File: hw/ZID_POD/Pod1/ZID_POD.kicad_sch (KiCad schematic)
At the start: 2 parts, among them J1 Z80-POD

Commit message: POD PCB 4 layouts
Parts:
- Z80-SKT1: renamed from SKT1; footprint Package_DIP:DIP-40_W15.24mm -> Package_DIP:DIP-40_W15.24mm_Socket; PIN_NOTE BIDIRECTIONAL pins are OUT on Z80, IN on DEBUGGER -> BIDIRECTIONAL pins are OUT on Z80, IN on TARGET
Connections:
- net GND: now also J1.30 (GND/NC)
- net PWR: no longer names the net of Z80-SKT1.11 (GND/NC)
- net PWR: no longer J1.30 (5V)
- no-connect marks 0 -> 1
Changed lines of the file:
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@@
 	(title_block
 		(title "ZID POD (1)")
-		(date "2026-04-10")
+		(date "2026-04-13")
 		(rev "PR1.0")
 		(company "SilkyDESIGN")
 		(comment 1 "Copyright 2026 AESilky")
+		(comment 3 "Z80 positions/orientations.")
+		(comment 4 "Layout 1 of 4 to accommodate different")
 	)
 	(text_box "NOTE: The ZID uses a FFC/FPC cable to connect to the POD. The Z80 signals are 1:1 on the ZID. Since the FFC cable is single side, it means the signal to pin on the POD connector are 1:40/40:1.\nThe Z80 Socket/Pins are 1:1. So, Pin-1 on the POD connector goes to Pin-40 on the Z80 Socket."
@@
 		)
 	)
+	(no_connect
+		(at 166.37 107.95)
+	)
 	(wire
 		(pts
@@
 		(pts
 			(xy 189.23 100.33) (xy 196.85 100.33)
-		)
-		(stroke
-			(width 0)
-			(type default)
-		)
-	)
-	(wire
-		(pts
-			(xy 158.75 107.95) (xy 166.37 107.95)
 		)
 		(stroke
@@
 		)
 	)
-	(label "PWR"
+	(label "GND"
 		(at 123.19 107.95 180)
 		(effects
@@
 			)
 			(justify right bottom)
-		)
-	)
-	(label "PWR"
-		(at 158.75 107.95 0)
-		(effects
-			(font
-				(size 1.27 1.27)
-			)
-			(justify left bottom)
 		)
 	)
@@
 		(on_board yes)
 		(dnp no)
-		(property "Reference" "SKT1"
+		(property "Reference" "Z80-SKT1"
 			(at 177.8 105.41 0)
 			(effects
@@
 			)
 		)
-		(property "Footprint" "Package_DIP:DIP-40_W15.24mm"
+		(property "Footprint" "Package_DIP:DIP-40_W15.24mm_Socket"
 			(at 177.8 105.41 0)
 			(effects
@@
 			)
 		)
-		(property "Description" "Plugs into the Z80 socket on target"
+		(property "Description" "Connect Z80 to Target via Cable"
 			(at 177.8 105.41 0)
 			(effects
@@
 			)
 		)
-		(property "PIN_NOTE" "BIDIRECTIONAL pins are OUT on Z80, IN on DEBUGGER"
+		(property "PIN_NOTE" "BIDIRECTIONAL pins are OUT on Z80, IN on TARGET"
 			(at 177.8 105.41 0)
 			(effects
@@
 			(project ""
 				(path "/5064845c-49f8-454d-ae5f-d06818afd8fe"
-					(reference "SKT1")
+					(reference "Z80-SKT1")
 					(unit 1)
 				)

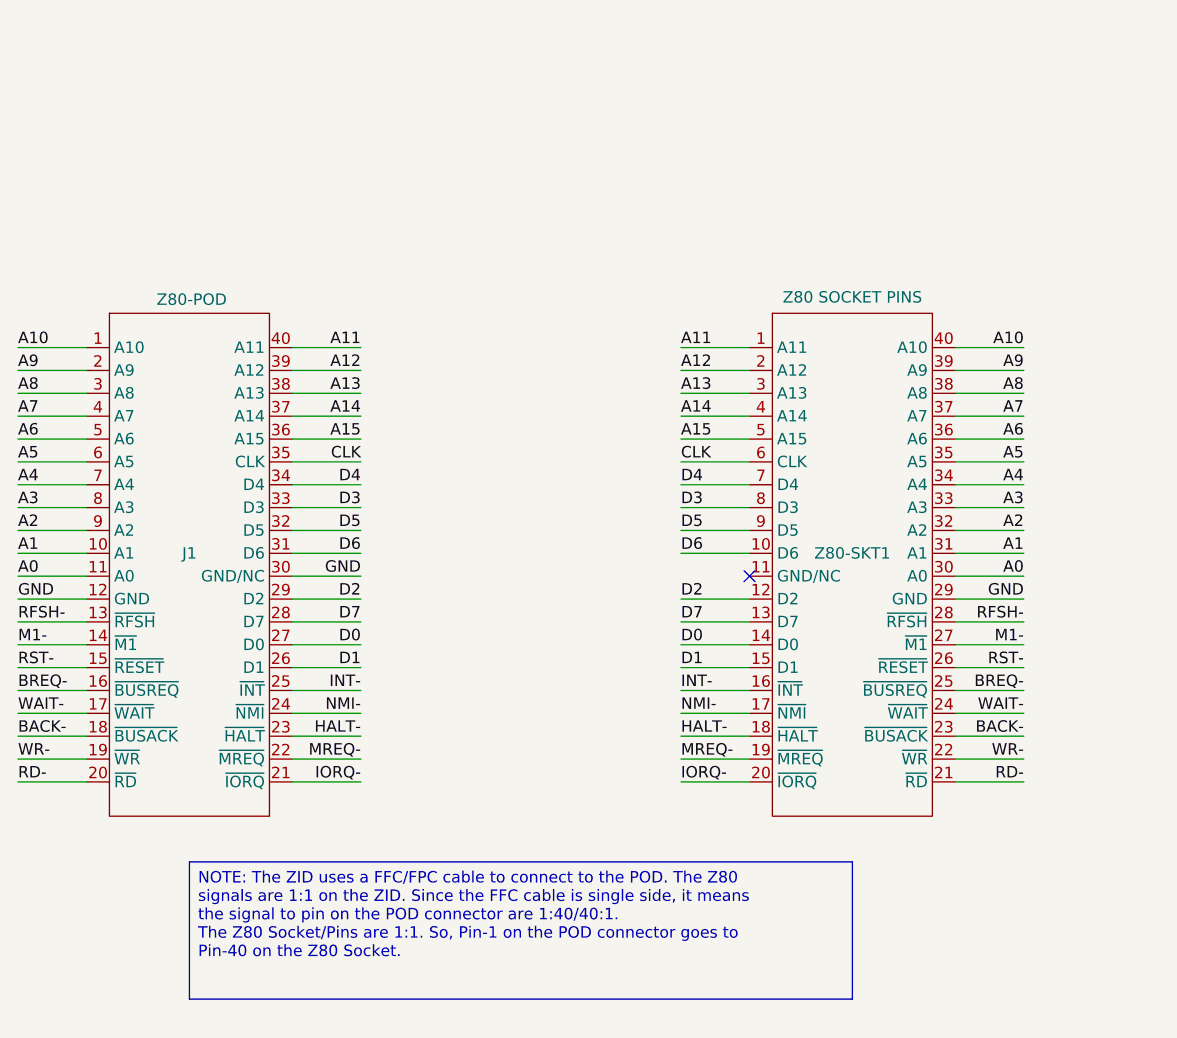
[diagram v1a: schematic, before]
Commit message: Change ZID,POD,ExpBP connector to SIP
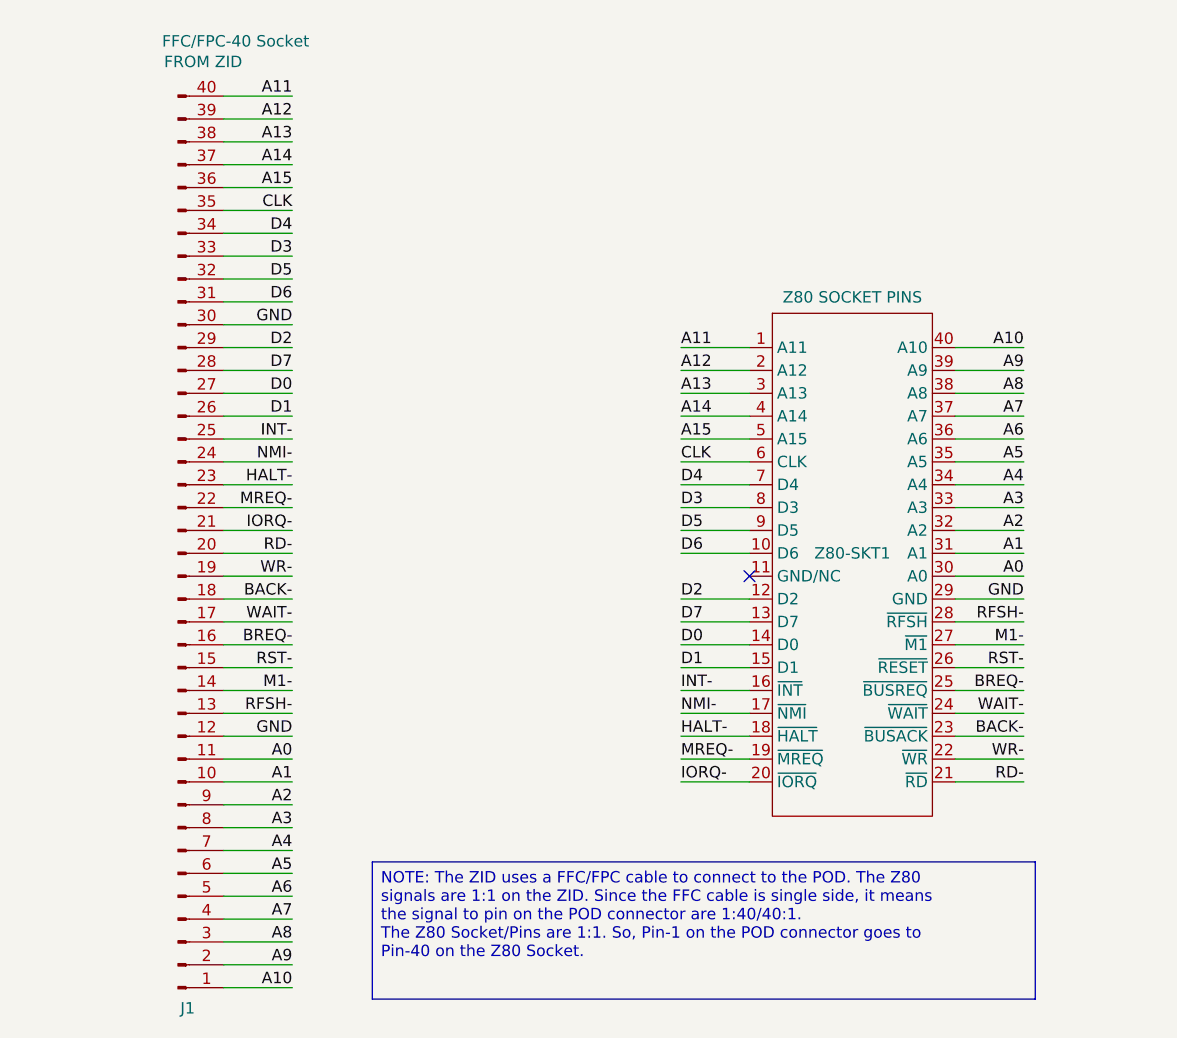
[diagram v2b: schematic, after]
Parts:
- removed J1: Z80-POD, AES_Library:CviLux_CF25401D0-05-NH_FFC-FPC-AES, symbol AES_Library:Z80-Pod-AES
- added J1: FFC/FPC-40 Socket, AES_Library:CviLux_CF25401D0-05-NH_FFC-FPC-AES, symbol Connector:Conn_01x40_Pin
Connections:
- net A0: now also J1.11 (Pin_11)
- net A1: now also J1.10 (Pin_10)
- net A10: now also J1.1 (Pin_1)
- net A11: now also J1.40 (Pin_40)
- net A12: now also J1.39 (Pin_39)
- net A13: now also J1.38 (Pin_38)
- net A14: now also J1.37 (Pin_37)
- net A15: now also J1.36 (Pin_36)
- net A2: now also J1.9 (Pin_9)
- net A3: now also J1.8 (Pin_8)
- net A4: now also J1.7 (Pin_7)
- net A5: now also J1.6 (Pin_6)
- net A6: now also J1.5 (Pin_5)
- net A7: now also J1.4 (Pin_4)
- net A8: now also J1.3 (Pin_3)
- net A9: now also J1.2 (Pin_2)
- net BACK-: now also J1.18 (Pin_18)
- net BREQ-: now also J1.16 (Pin_16)
- net CLK: now also J1.35 (Pin_35)
- net D0: now also J1.27 (Pin_27)
- net D1: now also J1.26 (Pin_26)
- net D2: now also J1.29 (Pin_29)
- net D3: now also J1.33 (Pin_33)
- net D4: now also J1.34 (Pin_34)
- net D5: now also J1.32 (Pin_32)
- net D6: now also J1.31 (Pin_31)
- net D7: now also J1.28 (Pin_28)
- net GND: now also J1.12 (Pin_12), J1.30 (Pin_30)
- net HALT-: now also J1.23 (Pin_23)
- net INT-: now also J1.25 (Pin_25)
- net IORQ-: now also J1.21 (Pin_21)
- net M1-: now also J1.14 (Pin_14)
- net MREQ-: now also J1.22 (Pin_22)
- net NMI-: now also J1.24 (Pin_24)
- net RD-: now also J1.20 (Pin_20)
- net RFSH-: now also J1.13 (Pin_13)
- net RST-: now also J1.15 (Pin_15)
- net WAIT-: now also J1.17 (Pin_17)
- net WR-: now also J1.19 (Pin_19)

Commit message: 74FCT541 to 74FCT2245. Move GND around CLK on ZID-POD connector
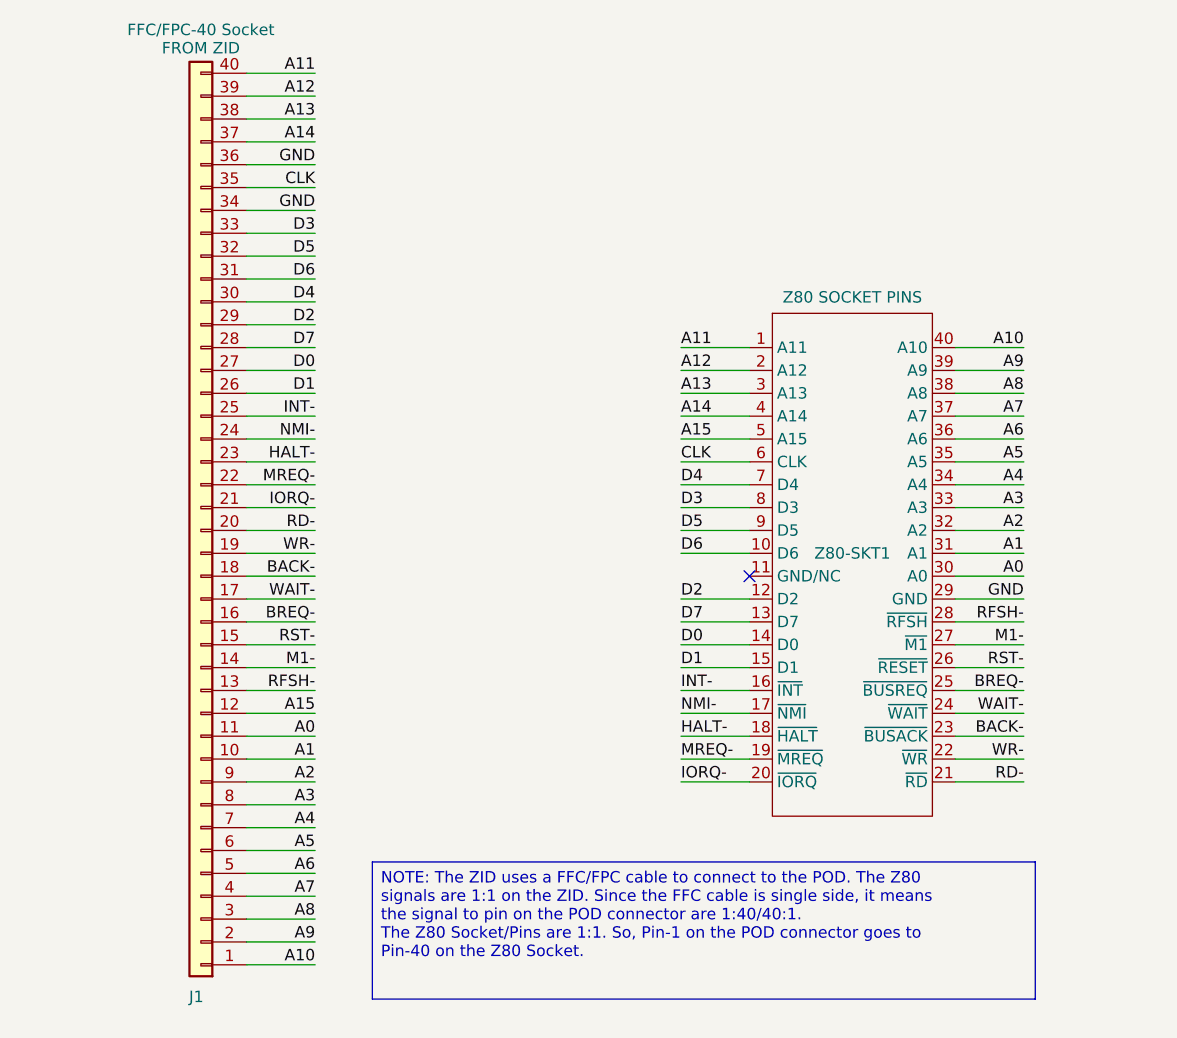
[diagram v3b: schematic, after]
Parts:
- removed J1: FFC/FPC-40 Socket, AES_Library:CviLux_CF25401D0-05-NH_FFC-FPC-AES, symbol Connector:Conn_01x40_Pin
- added J1: FFC/FPC-40 Socket, symbol Connector_Generic:Conn_01x40
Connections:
- net A0: now also J1.11 (Pin_11)
- net A1: now also J1.10 (Pin_10)
- net A10: now also J1.1 (Pin_1)
- net A11: now also J1.40 (Pin_40)
- net A12: now also J1.39 (Pin_39)
- net A13: now also J1.38 (Pin_38)
- net A14: now also J1.37 (Pin_37)
- net A15: now also J1.12 (Pin_12)
- net A2: now also J1.9 (Pin_9)
- net A3: now also J1.8 (Pin_8)
- net A4: now also J1.7 (Pin_7)
- net A5: now also J1.6 (Pin_6)
- net A6: now also J1.5 (Pin_5)
- net A7: now also J1.4 (Pin_4)
- net A8: now also J1.3 (Pin_3)
- net A9: now also J1.2 (Pin_2)
- net BACK-: now also J1.18 (Pin_18)
- net BREQ-: now also J1.16 (Pin_16)
- net CLK: now also J1.35 (Pin_35)
- net D0: now also J1.27 (Pin_27)
- net D1: now also J1.26 (Pin_26)
- net D2: now also J1.29 (Pin_29)
- net D3: now also J1.33 (Pin_33)
- net D4: now also J1.30 (Pin_30)
- net D5: now also J1.32 (Pin_32)
- net D6: now also J1.31 (Pin_31)
- net D7: now also J1.28 (Pin_28)
- net GND: now also J1.34 (Pin_34), J1.36 (Pin_36)
- net HALT-: now also J1.23 (Pin_23)
- net INT-: now also J1.25 (Pin_25)
- net IORQ-: now also J1.21 (Pin_21)
- net M1-: now also J1.14 (Pin_14)
- net MREQ-: now also J1.22 (Pin_22)
- net NMI-: now also J1.24 (Pin_24)
- net RD-: now also J1.20 (Pin_20)
- net RFSH-: now also J1.13 (Pin_13)
- net RST-: now also J1.15 (Pin_15)
- net WAIT-: now also J1.17 (Pin_17)
- net WR-: now also J1.19 (Pin_19)

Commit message: HW: Ready to lay out.
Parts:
- J1: footprint (none) -> AES_Library:CviLux_CF25401D0-05-NH_FFC-FPC-AES
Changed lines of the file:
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@@
 		)
 		(instances
-			(project ""
+			(project "ZID_POD"
 				(path "/5064845c-49f8-454d-ae5f-d06818afd8fe"
 					(reference "Z80-SKT1")
@@
 			)
 		)
-		(property "Footprint" ""
+		(property "Footprint" "AES_Library:CviLux_CF25401D0-05-NH_FFC-FPC-AES"
 			(at 105.41 102.87 0)
 			(effects
